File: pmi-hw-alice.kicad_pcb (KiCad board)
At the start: 2 copper layers, 64.8 x 20.3 mm, 36 parts, among them J1 Pmod-Interface-I2C6-In, J2 Pmod-Interface-I2C6-Out, J3 Board Conn, J4 Board Conn, U1 MCP23017-E/SO

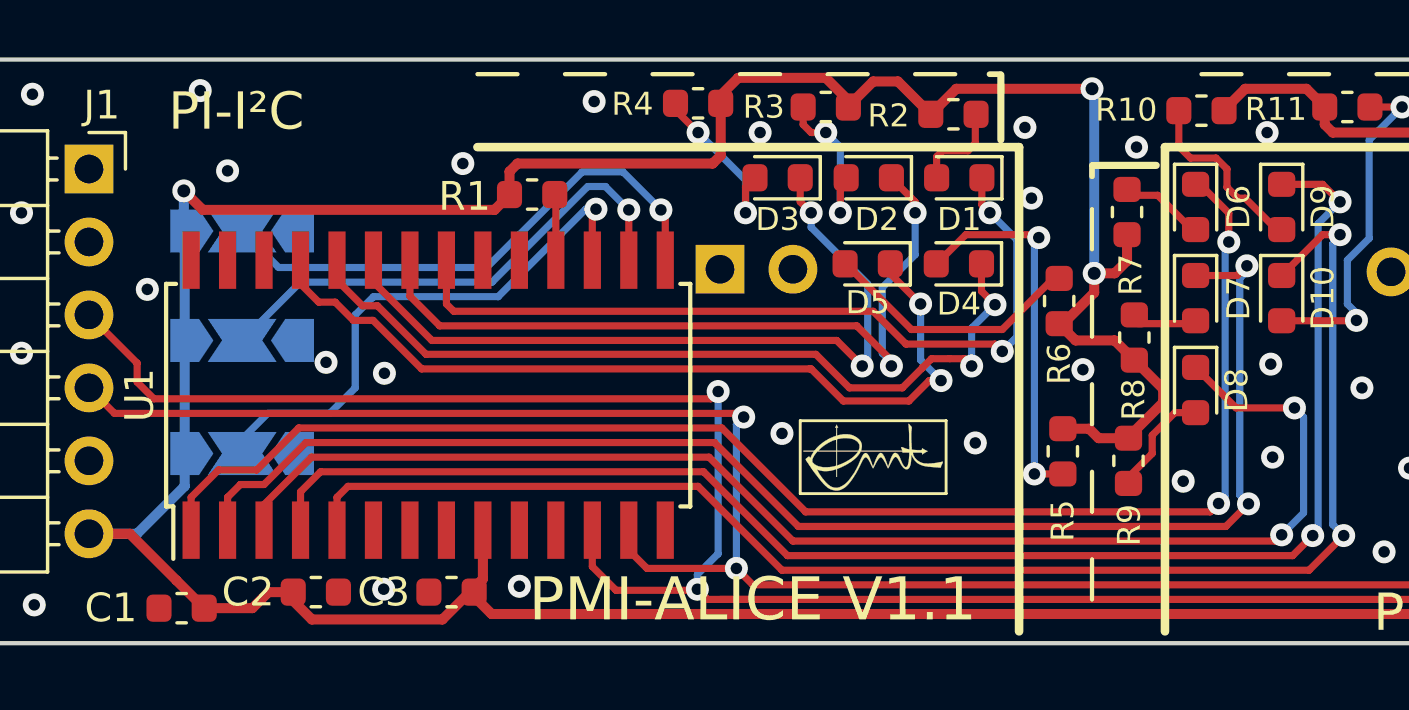
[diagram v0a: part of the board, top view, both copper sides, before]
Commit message: Bump to V1.2
* Add reset bridge to be able to reset the ic at power up
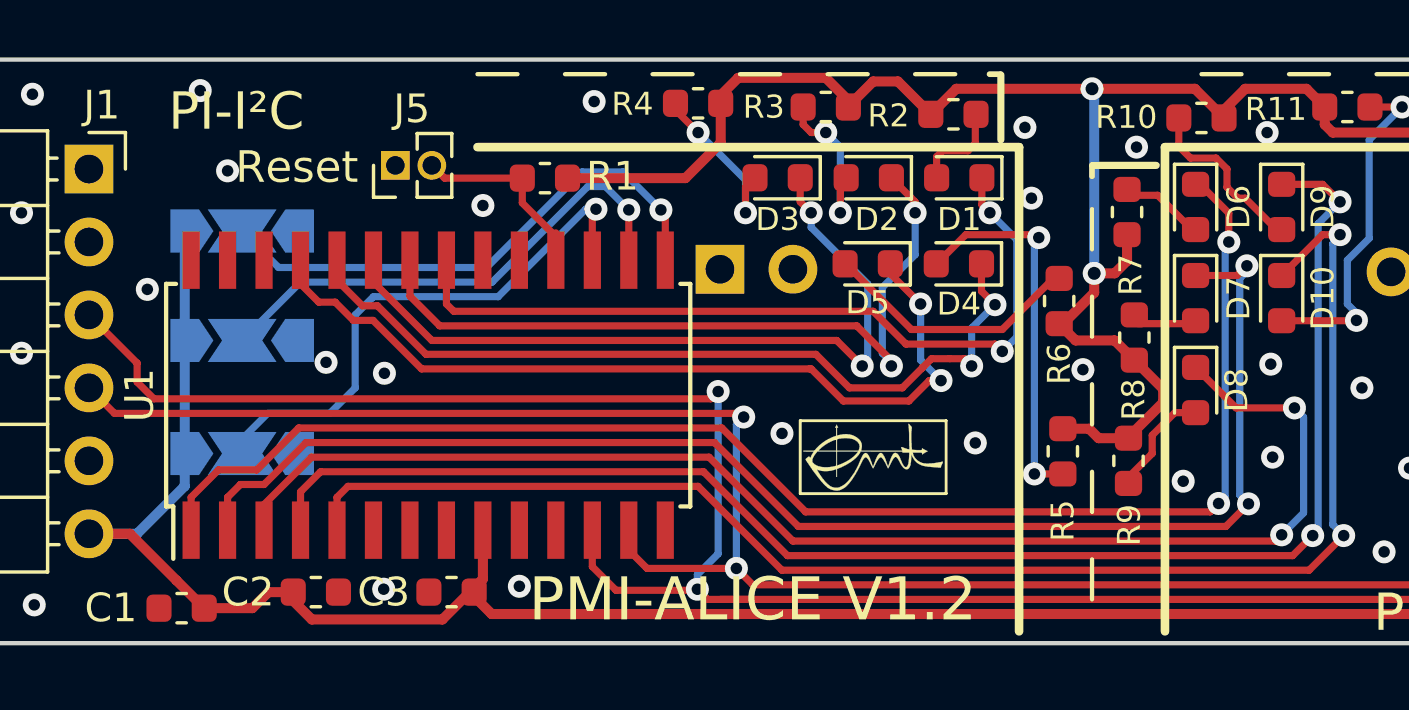
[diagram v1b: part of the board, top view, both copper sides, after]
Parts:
- added J5: Reset, Connector_PinHeader_1.27mm:PinHeader_1x02_P1.27mm_Vertical, F.Cu at (70.9, 58.3)
- moved R1 0.72 mm to (76.1, 58.7), turned to 180 degrees
- moved R10 0.25 mm to (98.9, 56.6)
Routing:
- net +3V3: track 164.1 -> 152.9 mm, vias 4 -> 3
- net Net-(J5-Pad2): track 2.30 -> 7.63 mm
- net GND: vias 37 -> 36
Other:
- board text added: "PMI-ALICE V1.2"
- board text added: "PMI-ALICE V1.2 2021"
- board text added: "Reset"
- board text removed: "PMI-ALICE V1.1"
- board text removed: "PMI-ALICE V1.1 2021"

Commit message: Bump to V1.3
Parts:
- turned R4 to 0 degrees
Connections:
- J1 pad 1: (no net) -> unconnected-(J1-Pad1)
- J1 pad 2: (no net) -> unconnected-(J1-Pad2)
- J2 pad 1: (no net) -> unconnected-(J2-Pad1)
- J2 pad 2: (no net) -> unconnected-(J2-Pad2)
- J3 pad 1: (no net) -> unconnected-(J3-Pad1)
- J3 pad 2: (no net) -> unconnected-(J3-Pad2)
- J4 pad 1: (no net) -> unconnected-(J4-Pad1)
- J4 pad 2: (no net) -> unconnected-(J4-Pad2)
- U1 pad 11: (no net) -> unconnected-(U1-Pad11)
- U1 pad 14: (no net) -> unconnected-(U1-Pad14)
- U1 pad 19: (no net) -> unconnected-(U1-Pad19)
- U1 pad 20: (no net) -> unconnected-(U1-Pad20)
- U1 pad 26: (no net) -> unconnected-(U1-Pad26)
- U1 pad 27: (no net) -> unconnected-(U1-Pad27)
- U1 pad 28: (no net) -> unconnected-(U1-Pad28)
- U1 pad 6: (no net) -> unconnected-(U1-Pad6)
- U1 pad 7: (no net) -> unconnected-(U1-Pad7)
- U1 pad 8: (no net) -> unconnected-(U1-Pad8)
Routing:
- net Net-(D3-Pad2): track 6.52 -> 3.19 mm, vias 2 -> 0
- net +3V3: track 152.9 -> 150.8 mm
- net /SCL: track 75.7 -> 73.7 mm
- net /D_MP_G: track 30.0 -> 28.7 mm
- net Net-(J5-Pad2): track 7.63 -> 6.67 mm
- net /D_MS_G: track 26.6 -> 25.8 mm
- net /D_MP_R: track 29.0 -> 28.3 mm
- net /SDA: track 68.6 -> 67.9 mm
- net /A2: track 19.5 -> 19.0 mm
- net GND: vias 36 -> 37
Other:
- outline, holes or cut-outs redrawn
- net class Default removed
- net class Supply removed
- board text added: "PMI-ALICE V1.3"
- board text added: "PMI-ALICE V1.3 2023"
- board text removed: "PMI-ALICE V1.0"
- board text removed: "PMI-ALICE V1.2"
- board text removed: "PMI-ALICE V1.2 2021"
